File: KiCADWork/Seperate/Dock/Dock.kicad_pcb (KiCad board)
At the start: 2 copper layers, 54.4 x 42.8 mm, 77 parts, among them J1 USB_C_Receptacle, J4 Conn_01x10_Socket, P1 USB_C_Plug, P2 USB_C_Plug, U1 USB2422T-I/MJ, U2 TPS61023DRLR, U3 AMS1117-3.3, U4 BQ24073RGT, U5 SIP32509DT-T1-GE3, U6 SIP32509DT-T1-GE3, Y1 X322524MOB4SI

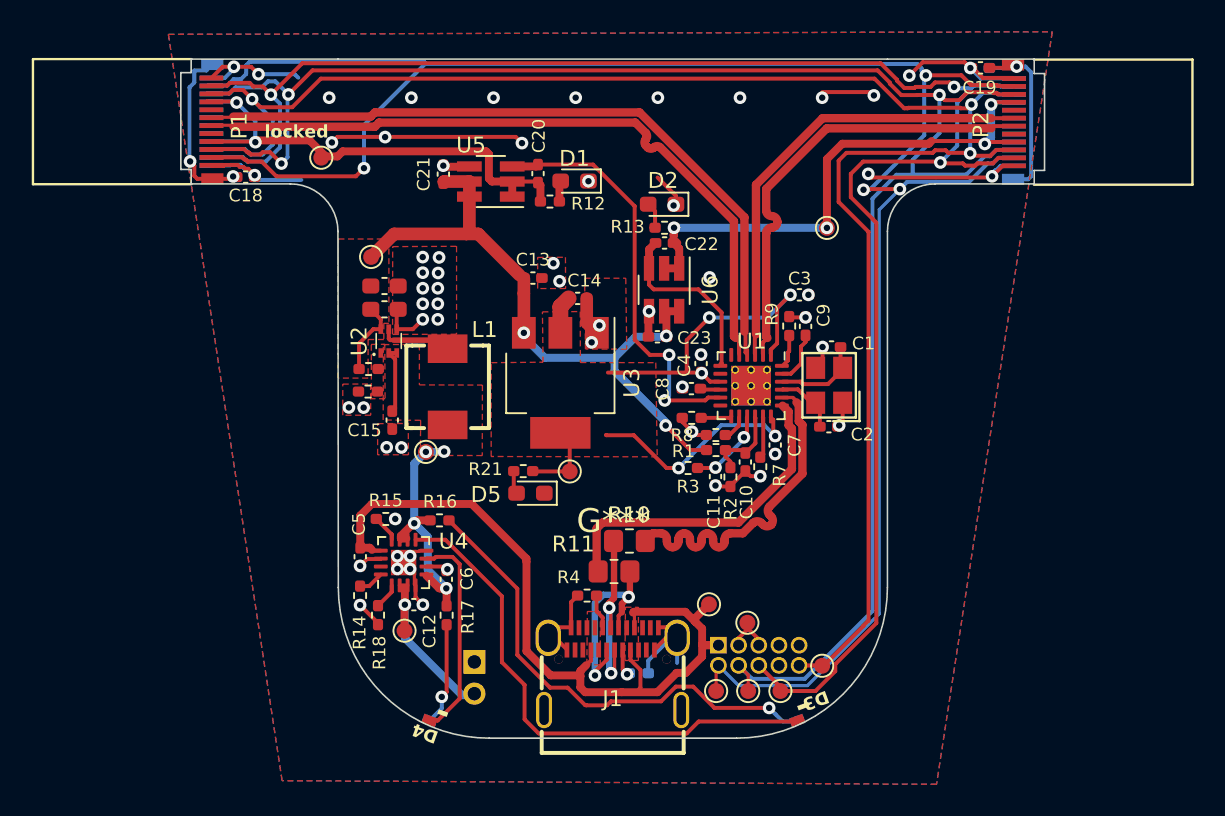
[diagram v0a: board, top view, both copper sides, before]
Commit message: Completing the combined layout
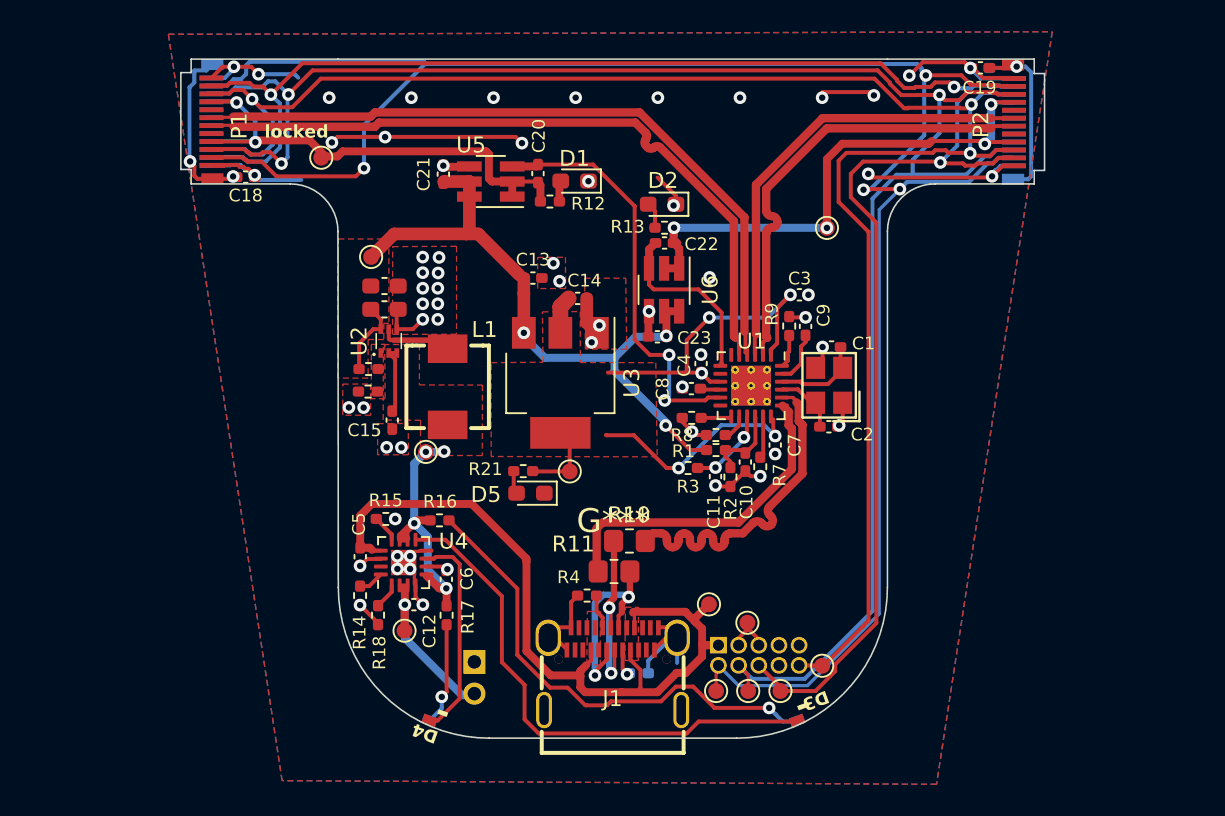
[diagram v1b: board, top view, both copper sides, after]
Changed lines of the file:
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@@
     (pad "17" smd rect locked (at 0 0 90) (size 1.6 1.6) (layers "F.Cu" "F.Mask")
       (net 1 "GND") (pinfunction "VSS") (pintype "passive"))
-    (model "${KICAD7_3DMODEL_DIR}/Package_DFN_QFN.3dshapes/QFN-16-1EP_3x3mm_P0.5mm_EP1.8x1.8mm.step"
+    (model "${KICAD6_3DMODEL_DIR}/Package_DFN_QFN.3dshapes/VQFN-16-1EP_3x3mm_P0.5mm_EP1.6x1.6mm.wrl"
       (offset (xyz 0 0 0))
       (scale (xyz 1 1 1))
@@
     )
     (fp_line (start -3.94 1.28) (end -3.94 11.27)
-      (stroke (width 0.15) (type solid)) (layer "F.SilkS"))
+      (stroke (width 0.15) (type solid)) (layer "Dwgs.User"))
     (fp_line (start -3.94 11.27) (end 3.94 11.27)
-      (stroke (width 0.15) (type solid)) (layer "F.SilkS"))
+      (stroke (width 0.15) (type solid)) (layer "Dwgs.User"))
     (fp_line (start 3.94 1.28) (end 3.94 11.27)
-      (stroke (width 0.15) (type solid)) (layer "F.SilkS"))
+      (stroke (width 0.15) (type solid)) (layer "Dwgs.User"))
     (fp_arc (start -2.79 1.98) (mid -2.973847 1.903848) (end -3.05 1.72)
       (stroke (width 0.15) (type solid)) (layer "Dwgs.User"))
@@
     )
     (fp_line (start -3.94 1.28) (end -3.94 11.27)
-      (stroke (width 0.15) (type solid)) (layer "F.SilkS"))
+      (stroke (width 0.15) (type solid)) (layer "Dwgs.User"))
     (fp_line (start -3.94 11.27) (end 3.94 11.27)
-      (stroke (width 0.15) (type solid)) (layer "F.SilkS"))
+      (stroke (width 0.15) (type solid)) (layer "Dwgs.User"))
     (fp_line (start 3.94 1.28) (end 3.94 11.27)
-      (stroke (width 0.15) (type solid)) (layer "F.SilkS"))
+      (stroke (width 0.15) (type solid)) (layer "Dwgs.User"))
     (fp_arc (start -2.79 1.98) (mid -2.973847 1.903848) (end -3.05 1.72)
       (stroke (width 0.15) (type solid)) (layer "Dwgs.User"))
@@
     (pad "24" smd roundrect locked (at -1.25 -1.9375 270) (size 0.25 0.875) (layers "F.Cu" "F.Paste" "F.Mask") (roundrect_rratio 0.25)
       (net 47 "Net-(U1-RBIAS)") (pinfunction "RBIAS") (pintype "unspecified"))
-    (pad "25" thru_hole circle locked (at -1 -1 270) (size 0.5 0.5) (drill 0.3) (layers "*.Cu")
-      (net 1 "GND") (pinfunction "EP") (pintype "unspecified") (zone_connect 2))
-    (pad "25" thru_hole circle locked (at -1 0 270) (size 0.5 0.5) (drill 0.3) (layers "*.Cu")
-      (net 1 "GND") (pinfunction "EP") (pintype "unspecified") (zone_connect 2))
-    (pad "25" thru_hole circle locked (at -1 1 270) (size 0.5 0.5) (drill 0.3) (layers "*.Cu")
-      (net 1 "GND") (pinfunction "EP") (pintype "unspecified") (zone_connect 2))
-    (pad "25" thru_hole circle locked (at 0 -1 270) (size 0.5 0.5) (drill 0.3) (layers "*.Cu")
-      (net 1 "GND") (pinfunction "EP") (pintype "unspecified") (zone_connect 2))
-    (pad "25" thru_hole circle locked (at 0 0 270) (size 0.5 0.5) (drill 0.3) (layers "*.Cu")
-      (net 1 "GND") (pinfunction "EP") (pintype "unspecified") (zone_connect 2))
+    (pad "25" thru_hole circle locked (at -1 -1 270) (size 0.5 0.5) (drill 0.2) (layers "*.Cu")
+      (net 1 "GND") (pinfunction "EP") (pintype "unspecified"))
+    (pad "25" thru_hole circle locked (at -1 0 270) (size 0.5 0.5) (drill 0.2) (layers "*.Cu")
+      (net 1 "GND") (pinfunction "EP") (pintype "unspecified"))
+    (pad "25" thru_hole circle locked (at -1 1 270) (size 0.5 0.5) (drill 0.2) (layers "*.Cu")
+      (net 1 "GND") (pinfunction "EP") (pintype "unspecified"))
+    (pad "25" thru_hole circle locked (at 0 -1 270) (size 0.5 0.5) (drill 0.2) (layers "*.Cu")
+      (net 1 "GND") (pinfunction "EP") (pintype "unspecified"))
+    (pad "25" thru_hole circle locked (at 0 0 270) (size 0.5 0.5) (drill 0.2) (layers "*.Cu")
+      (net 1 "GND") (pinfunction "EP") (pintype "unspecified"))
     (pad "25" smd rect locked (at 0 0 270) (size 2.5 2.5) (layers "F.Cu" "F.Mask")
       (net 1 "GND") (pinfunction "EP") (pintype "unspecified"))
     (pad "25" smd rect locked (at 0 0 270) (size 2.5 2.5) (layers "B.Cu")
-      (net 1 "GND") (pinfunction "EP") (pintype "unspecified") (zone_connect 2) (thermal_bridge_angle 45))
-    (pad "25" thru_hole circle locked (at 0 1 270) (size 0.5 0.5) (drill 0.3) (layers "*.Cu")
-      (net 1 "GND") (pinfunction "EP") (pintype "unspecified") (zone_connect 2))
-    (pad "25" thru_hole circle locked (at 1 -1 270) (size 0.5 0.5) (drill 0.3) (layers "*.Cu")
-      (net 1 "GND") (pinfunction "EP") (pintype "unspecified") (zone_connect 2))
-    (pad "25" thru_hole circle locked (at 1 0 270) (size 0.5 0.5) (drill 0.3) (layers "*.Cu")
-      (net 1 "GND") (pinfunction "EP") (pintype "unspecified") (zone_connect 2))
-    (pad "25" thru_hole circle locked (at 1 1 270) (size 0.5 0.5) (drill 0.3) (layers "*.Cu")
-      (net 1 "GND") (pinfunction "EP") (pintype "unspecified") (zone_connect 2))
-    (model "${KICAD7_3DMODEL_DIR}/Package_DFN_QFN.3dshapes/QFN-24-1EP_4x4mm_P0.5mm_EP2.6x2.6mm.step"
+      (net 1 "GND") (pinfunction "EP") (pintype "unspecified"))
+    (pad "25" thru_hole circle locked (at 0 1 270) (size 0.5 0.5) (drill 0.2) (layers "*.Cu")
+      (net 1 "GND") (pinfunction "EP") (pintype "unspecified"))
+    (pad "25" thru_hole circle locked (at 1 -1 270) (size 0.5 0.5) (drill 0.2) (layers "*.Cu")
+      (net 1 "GND") (pinfunction "EP") (pintype "unspecified"))
+    (pad "25" thru_hole circle locked (at 1 0 270) (size 0.5 0.5) (drill 0.2) (layers "*.Cu")
+      (net 1 "GND") (pinfunction "EP") (pintype "unspecified"))
+    (pad "25" thru_hole circle locked (at 1 1 270) (size 0.5 0.5) (drill 0.2) (layers "*.Cu")
+      (net 1 "GND") (pinfunction "EP") (pintype "unspecified"))
+    (model "${KICAD6_3DMODEL_DIR}/Package_DFN_QFN.3dshapes/HVQFN-24-1EP_4x4mm_P0.5mm_EP2.5x2.5mm.wrl"
       (offset (xyz 0 0 0))
       (scale (xyz 1 1 1))
@@
     (model "C:/BLEEarrings/CADWork/USB-C/USBC.step"
       (offset (xyz 0 -1.2 1.6))
-      (scale (xyz 2.54 2.54 2.54))
+      (scale (xyz 1 1 1))
       (rotate (xyz -90 0 180))
     )
